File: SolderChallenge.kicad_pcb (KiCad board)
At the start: 2 copper layers, 50 x 100 mm, 36 parts, among them Q1 MOS_N, Q2 MOS_N, Q3 MOS_N, Q4 MOS_N_x2, U1 555, U2 555, U3 555

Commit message: Switch R4 and R5 for better routing
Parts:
- moved R4 4.00 mm to (98.0, 73.5)
- moved R5 4.00 mm to (98.0, 77.5)
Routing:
- net LED5_Vcc: track 61.8 -> 55.0 mm, vias 1 -> 0
- net LED4_Vcc: track 38.7 -> 42.7 mm
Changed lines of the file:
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@@
   )
   (module SolderChallenge:R_Axial_DIN0207_L6.3mm_D2.5mm_P7.62mm_Horizontal (layer F.Cu)
-    (at 98 77.5 180)
+    (at 98 73.5 180)
     (descr "Resistor, Axial_DIN0207 series, Axial, Horizontal, pin pitch=7.62mm, 0.25W = 1/4W, length*diameter=6.3*2.5mm^2, http://cdn-reichelt.de/documents/datenblatt/B400/1_4W%23YAG.pdf")
     (tags "Resistor Axial_DIN0207 series Axial Horizontal pin pitch 7.62mm 0.25W = 1/4W length 6.3mm diameter 2.5mm")
@@
   )
   (module SolderChallenge:R_Axial_DIN0207_L6.3mm_D2.5mm_P7.62mm_Horizontal (layer F.Cu)
-    (at 98 73.5 180)
+    (at 98 77.5 180)
     (descr "Resistor, Axial_DIN0207 series, Axial, Horizontal, pin pitch=7.62mm, 0.25W = 1/4W, length*diameter=6.3*2.5mm^2, http://cdn-reichelt.de/documents/datenblatt/B400/1_4W%23YAG.pdf")
     (tags "Resistor Axial_DIN0207 series Axial Horizontal pin pitch 7.62mm 0.25W = 1/4W length 6.3mm diameter 2.5mm")
@@
   (segment (start 88.25 112.75) (end 92.85 117.35) (width 0.25) (layer F.Cu) (net 12))
   (segment (start 92.85 117.35) (end 94.25 117.35) (width 0.25) (layer F.Cu) (net 12))
-  (segment (start 98 77.5) (end 97 78.5) (width 0.25) (layer F.Cu) (net 13))
-  (segment (start 97 78.5) (end 97 109.5) (width 0.25) (layer F.Cu) (net 13))
-  (segment (start 97 109.5) (end 94.25 112.25) (width 0.25) (layer F.Cu) (net 13))
+  (segment (start 98 73.5) (end 98 74.75) (width 0.25) (layer F.Cu) (net 13))
+  (segment (start 98 74.75) (end 96.75 76) (width 0.25) (layer F.Cu) (net 13))
+  (segment (start 96.75 76) (end 96.75 85.396998) (width 0.25) (layer F.Cu) (net 13))
+  (segment (start 96.75 85.396998) (end 96.765001 85.411999) (width 0.25) (layer F.Cu) (net 13))
+  (segment (start 96.765001 85.411999) (end 96.765001 86.588001) (width 0.25) (layer F.Cu) (net 13))
+  (segment (start 96.765001 86.588001) (end 96.75 86.603002) (width 0.25) (layer F.Cu) (net 13))
+  (segment (start 96.75 86.603002) (end 96.75 109.75) (width 0.25) (layer F.Cu) (net 13))
+  (segment (start 96.75 109.75) (end 94.25 112.25) (width 0.25) (layer F.Cu) (net 13))
   (segment (start 94.25 112.25) (end 94.25 114.65) (width 0.25) (layer F.Cu) (net 13))
   (segment (start 81.7 131.35) (end 83.6 131.35) (width 0.25) (layer F.Cu) (net 14))
@@
   (segment (start 84.25 132) (end 92.45 132) (width 0.25) (layer F.Cu) (net 14))
   (segment (start 92.45 132) (end 93.55 133.1) (width 0.25) (layer F.Cu) (net 14))
-  (segment (start 98 73.5) (end 96.86863 73.5) (width 0.25) (layer B.Cu) (net 15))
-  (segment (start 96.86863 73.5) (end 96.5 73.86863) (width 0.25) (layer B.Cu) (net 15))
-  (segment (start 96.5 73.86863) (end 96.5 79.25) (width 0.25) (layer B.Cu) (net 15))
-  (segment (start 96.5 79.25) (end 98.25 81) (width 0.25) (layer B.Cu) (net 15))
+  (segment (start 98 77.5) (end 98 81.25) (width 0.25) (layer F.Cu) (net 15))
+  (segment (start 98 81.25) (end 97.950001 81.299999) (width 0.25) (layer F.Cu) (net 15))
   (segment (start 97.5 81.75) (end 97.5 125) (width 0.25) (layer F.Cu) (net 15))
-  (segment (start 98.25 81) (end 97.950001 81.299999) (width 0.25) (layer F.Cu) (net 15))
   (segment (start 97.950001 81.299999) (end 97.5 81.75) (width 0.25) (layer F.Cu) (net 15))
-  (via (at 98.25 81) (size 0.6) (drill 0.4) (layers F.Cu B.Cu) (net 15))
-  (segment (start 98 73.5) (end 97.5 74) (width 0.25) (layer F.Cu) (net 15))
   (segment (start 94.25 128.25) (end 94.25 130.9) (width 0.25) (layer F.Cu) (net 15))
   (segment (start 97.5 125) (end 94.25 128.25) (width 0.25) (layer F.Cu) (net 15))

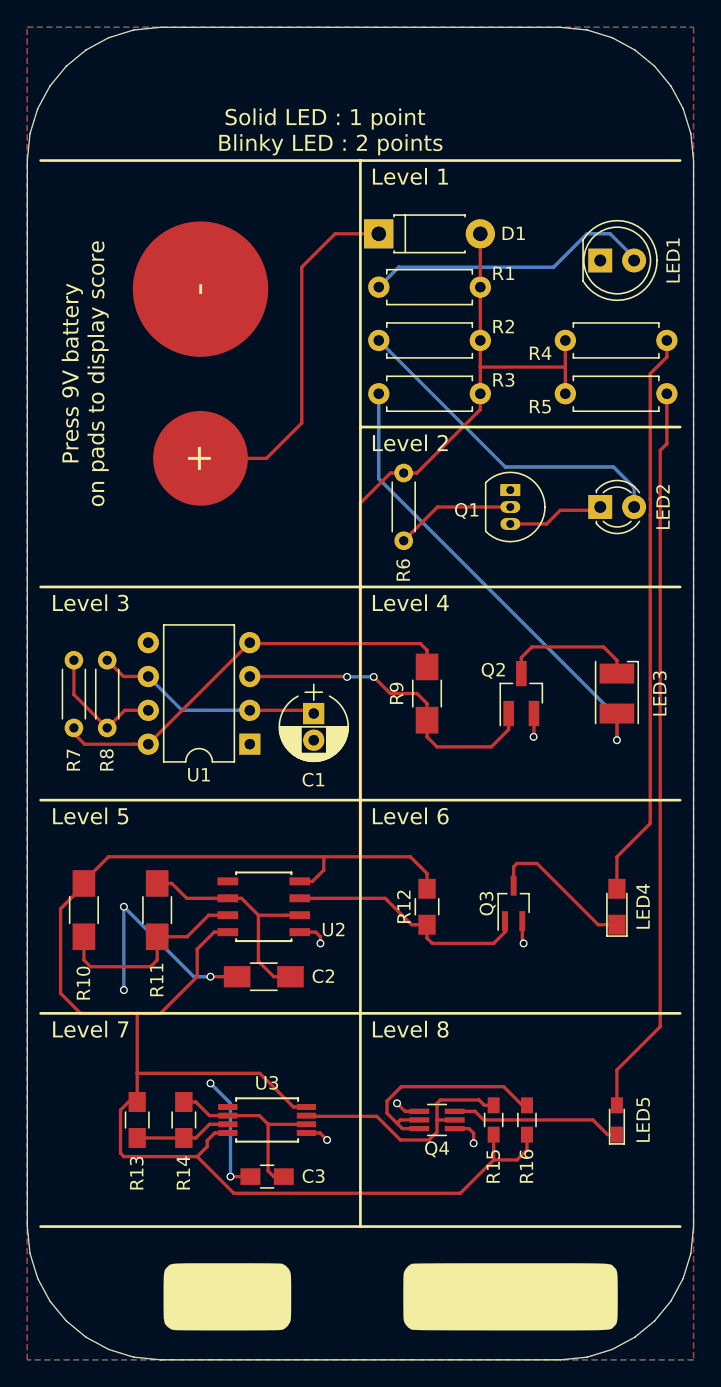
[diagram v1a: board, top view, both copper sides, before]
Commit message: Added diode polarity to silkscreen and made all LEDs have cathode at bottom
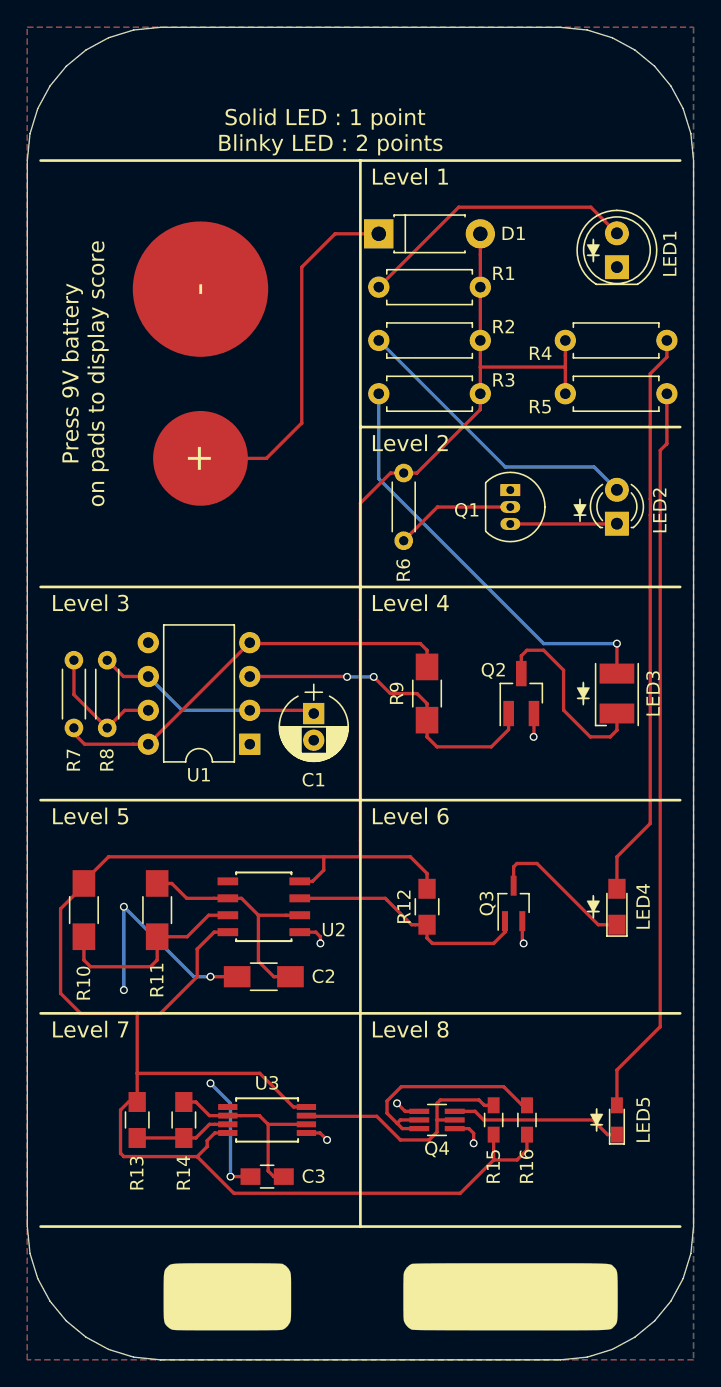
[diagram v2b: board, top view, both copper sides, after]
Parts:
- added G***: LOGO, SolderChallenge:0803_diode_silk, F.Cu at (92.5, 116.0)
- added G***: LOGO, SolderChallenge:0803_diode_silk, F.Cu at (92.8, 132.0)
- added G***: LOGO, SolderChallenge:0803_diode_silk, F.Cu at (91.8, 100.0)
- added G***: LOGO, SolderChallenge:0803_diode_silk, F.Cu at (91.5, 86.2)
- added G***: LOGO, SolderChallenge:0803_diode_silk, F.Cu at (92.5, 66.8)
- moved LED2 1.77 mm to (94.2, 87.2), turned to 90 degrees
- moved LED1 1.35 mm to (94.2, 68.0), turned to 90 degrees
- turned LED3 to 90 degrees
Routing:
- net Net-(LED3-Pad1): track 10.1 -> 14.6 mm
- net LED3_Vcc: track 35.4 -> 31.6 mm
- net LED2_Vcc: track 25.2 -> 22.5 mm
- net Net-(LED2-Pad1): track 7.28 -> 8.31 mm
- net Net-(LED1-Pad2): track 21.8 -> 21.2 mm

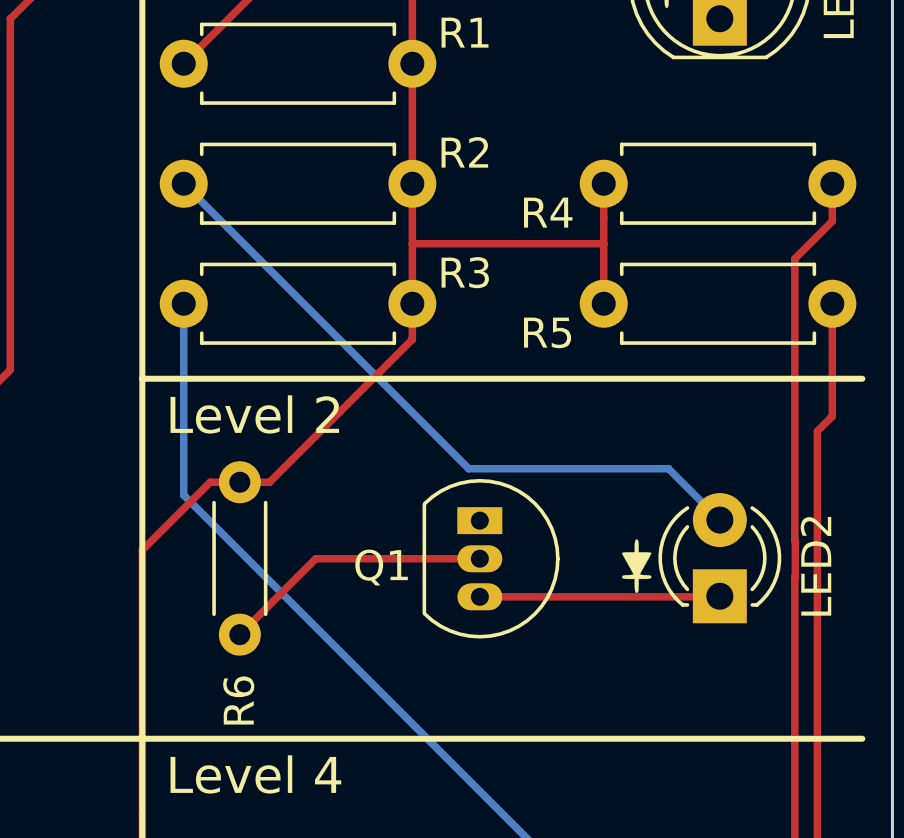
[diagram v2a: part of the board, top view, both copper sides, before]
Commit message: Modified Q1 to use wide variant of package as that's what I ordred. RS had wrong info on site.
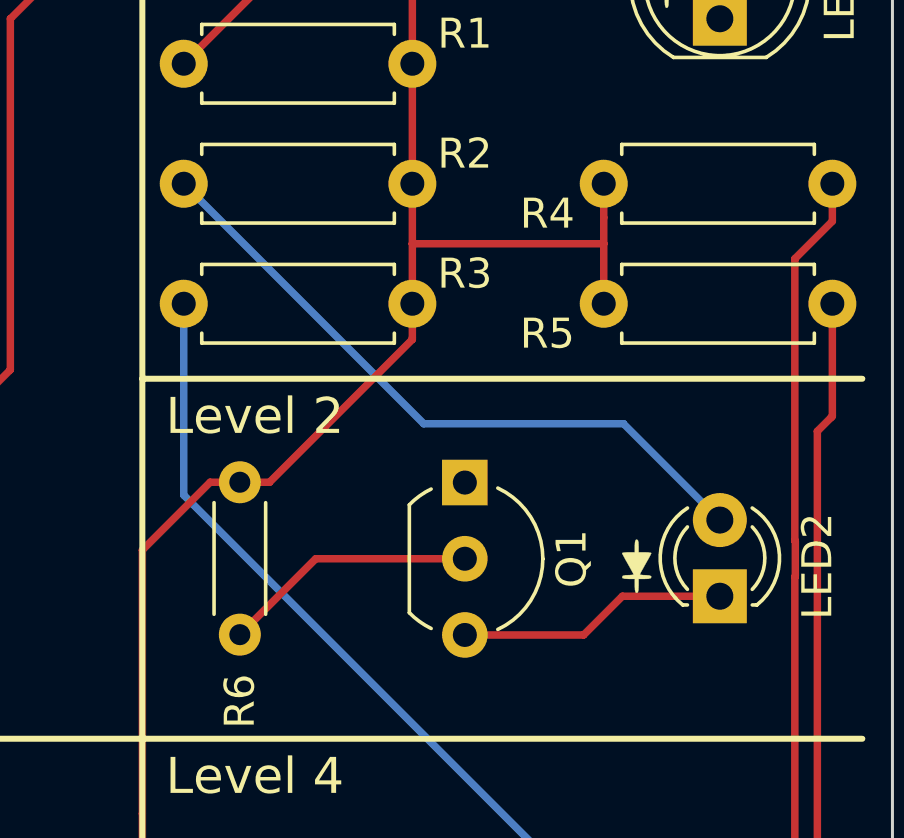
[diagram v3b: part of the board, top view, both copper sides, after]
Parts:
- Q1: footprint SolderChallenge:TO-92_Inline_Narrow_Oval_SGD -> SolderChallenge:TO-92_Inline_Wide_SGD
- moved Q1 1.36 mm to (85.8, 83.5)
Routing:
- net Net-(LED2-Pad1): track 8.31 -> 9.06 mm
- net Net-(Q1-PadG): track 9.05 -> 8.55 mm
